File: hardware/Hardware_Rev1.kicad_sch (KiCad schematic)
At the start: 148 parts, among them J1 RJ45_LED_Shielded, J2 6P6C, Q1 BSS138, Q10 AO3401A, Q11 AO3401A, Q12 AO3401A, Q13 BSS138, Q14 BSS138, Q15 BSS138, Q16 AO3401A, Q17 AO3401A, Q18 AO3401A, Q19 BSS138, Q2 BSS138, Q20 BSS138, Q21 BSS138, Q22 AO3401A, Q23 AO3401A, Q24 AO3401A, Q3 BSS138, Q4 AO3401A, Q5 AO3401A, Q6 AO3401A, Q7 BSS138, Q8 BSS138, Q9 BSS138, U1 OKI, U2 Teensy4.1_DEV-16771

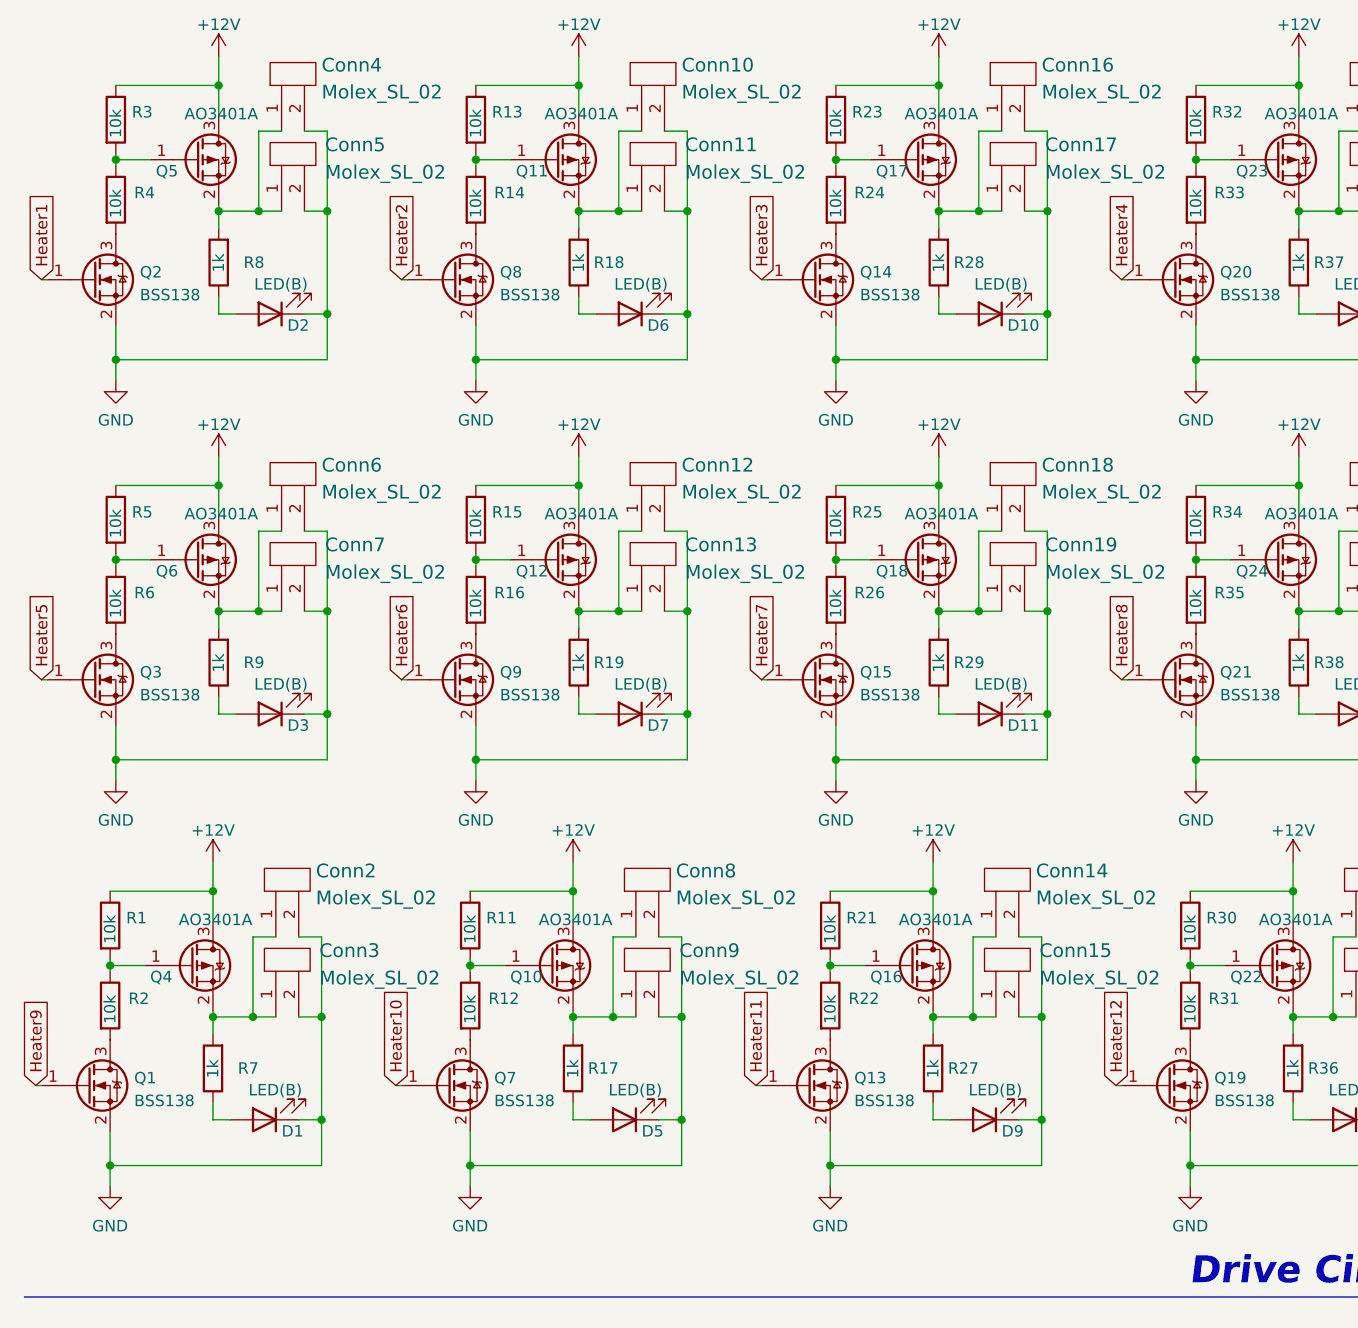
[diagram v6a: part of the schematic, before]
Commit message: Added pull down resistors
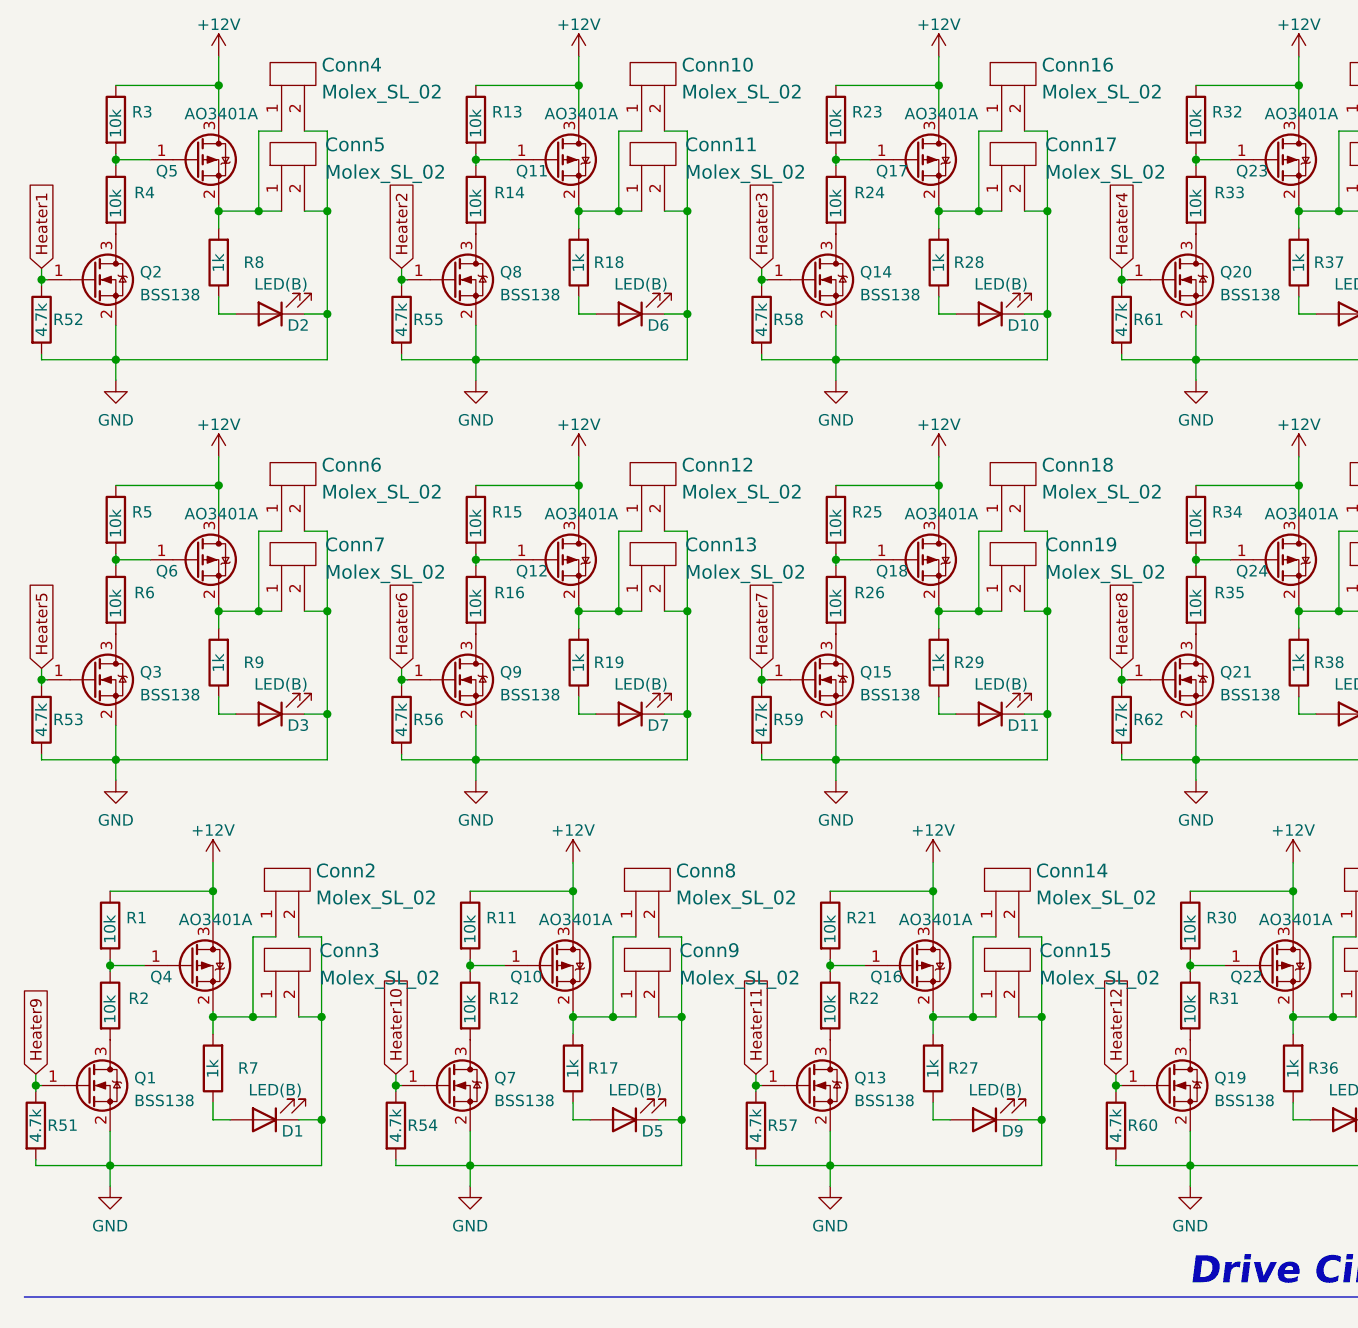
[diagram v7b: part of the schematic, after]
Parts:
- added R51, R52, R53, R54, R55, R56, R57, R58, R59, R60, R61, R62: 4.7k, Resistor_SMD:R_0603_1608Metric_Pad0.98x0.95mm_HandSolder, symbol Device:R
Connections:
- net GND: now also R51.2, R52.2, R53.2, R54.2, R55.2, R56.2, R57.2, R58.2, R59.2, R60.2, R61.2, R62.2
- net Heater1: now also R52.1
- net Heater10: now also R54.1
- net Heater11: now also R57.1
- net Heater12: now also R60.1
- net Heater2: now also R55.1
- net Heater3: now also R58.1
- net Heater4: now also R61.1
- net Heater5: now also R53.1
- net Heater6: now also R56.1
- net Heater7: now also R59.1
- net Heater8: now also R62.1
- net Heater9: now also R51.1

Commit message: Cleaned traces
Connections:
- net Heater1: now also U2.32 (OUT1B); no longer U2.2 (OUT2)
- net Heater10: now also U2.12 (MISO); no longer U2.25 (A11)
- net Heater11: now also U2.11 (MOSI); no longer U2.24 (A10)
- net Heater12: now also U2.10 (CS1); no longer U2.23 (A9)
- net Heater2: now also U2.31 (CTX3); no longer U2.6 (OUT1D)
- net Heater3: now also U2.30 (CRX3); no longer U2.9 (OUT1C)
- net Heater4: now also U2.29 (TX7); no longer U2.32 (OUT1B)
- net Heater5: now also U2.28 (RX7); no longer U2.12 (MISO)
- net Heater6: now also U2.27 (A13); no longer U2.11 (MOSI)
- net Heater7: now also U2.26 (A12); no longer U2.38 (A14)
- net Heater8: now also U2.25 (A11); no longer U2.27 (A13)
- net Heater9: now also U2.24 (A10); no longer U2.26 (A12)
- net Temp1: now also U2.38 (A14); no longer U2.14 (A0)
- net Temp10: now also U2.19 (A5); no longer U2.41 (A17)
- net Temp11: now also U2.20 (A6); no longer U2.40 (A16)
- net Temp12: now also U2.21 (A7); no longer U2.39 (A15)
- net Temp2: now also U2.39 (A15); no longer U2.15 (A1)
- net Temp3: now also U2.40 (A16); no longer U2.16 (A2)
- net Temp4: now also U2.41 (A17); no longer U2.17 (A3)
- net Temp5: now also U2.14 (A0); no longer U2.18 (A4)
- net Temp6: now also U2.15 (A1); no longer U2.19 (A5)
- net Temp7: now also U2.16 (A2); no longer U2.20 (A6)
- net Temp8: now also U2.17 (A3); no longer U2.21 (A7)
- net Temp9: now also U2.18 (A4); no longer U2.22 (A8)
- net at R40.2: now also U2.8 (TX2); no longer U2.1 (TX1)
- net at U2.0 (RX1): now also R47.2; no longer R39.2
- net at R43.2: now also U2.5 (IN2); no longer U2.28 (RX7)
- net at R44.2: now also U2.4 (BCLK2); no longer U2.29 (TX7)
- net at R49.2: now also U2.22 (A8); no longer U2.3 (LRCLK2)
- net at R48.2: now also U2.1 (TX1); no longer U2.31 (CTX3)
- net at R45.2: now also U2.3 (LRCLK2); no longer U2.34 (RX8)
- net at R46.2: now also U2.2 (OUT2); no longer U2.35 (TX8)
- net at R50.2: now also U2.23 (A9); no longer U2.4 (BCLK2)
- net at R42.2: now also U2.6 (OUT1D); no longer U2.8 (TX2)
- new net: R39.2, U2.9 (OUT1C)
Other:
- moved on the sheet: D15, D16, D17, D18, D19, D20, D21, D22, D23, D24, D25, D26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
